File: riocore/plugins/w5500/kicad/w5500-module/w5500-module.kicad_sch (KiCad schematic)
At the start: 2 parts, among them J15 Conn_01x06, J16 Conn_01x06

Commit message: kicad: recover positions
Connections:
- net spi_cs renamed sel
- net spi_miso renamed miso
- net spi_mosi renamed mosi
- net spi_sclk renamed sclk
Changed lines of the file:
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@@
 		)
 	)
-	(hierarchical_label "spi_miso"
+	(hierarchical_label "miso"
 		(shape input)
 		(at 130.81 92.71 180)
@@
 		)
 	)
-	(hierarchical_label "spi_sclk"
+	(hierarchical_label "sclk"
 		(shape input)
 		(at 162.56 97.79 0)
@@
 		)
 	)
-	(hierarchical_label "spi_cs"
+	(hierarchical_label "sel"
 		(shape input)
 		(at 162.56 95.25 0)
@@
 		)
 	)
-	(hierarchical_label "spi_mosi"
+	(hierarchical_label "mosi"
 		(shape input)
 		(at 162.56 100.33 0)

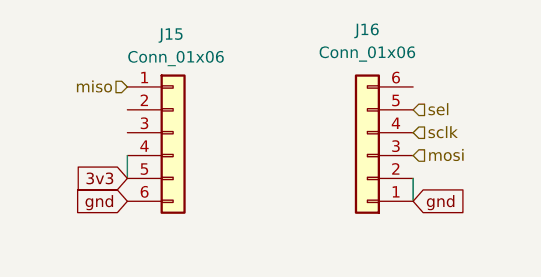
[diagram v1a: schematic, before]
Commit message: kicad: get power-signals
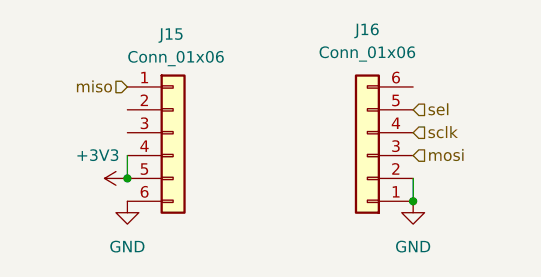
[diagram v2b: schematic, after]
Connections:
- net 3v3 renamed +3V3
- net gnd renamed GND
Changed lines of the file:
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@@
 	(generator_version "9.0")
 	(paper "A4")
+	(junction
+		(at 162.56 105.41)
+		(diameter 0)
+		(color 0 0 0 0)
+	)
+	(junction
+		(at 130.81 102.87)
+		(diameter 0)
+		(color 0 0 0 0)
+	)
 	(wire
 		(pts
@@
 			(width 0)
 			(type default)
-		)
-	)
-	(global_label "gnd"
-		(shape input)
-		(at 162.56 105.41 0)
-		(fields_autoplaced yes)
-		(effects
-			(font
-				(size 1.27 1.27)
-			)
-			(justify left)
-		)
-		(property "Intersheetrefs" "${INTERSHEET_REFS}"
-			(at 168.9128 105.41 0)
-			(effects
-				(font
-					(size 1.27 1.27)
-				)
-				(justify left)
-				(hide yes)
-			)
-		)
-	)
-	(global_label "3v3"
-		(shape input)
-		(at 130.81 102.87 180)
-		(fields_autoplaced yes)
-		(effects
-			(font
-				(size 1.27 1.27)
-			)
-			(justify right)
-		)
-		(property "Intersheetrefs" "${INTERSHEET_REFS}"
-			(at 124.5176 102.87 0)
-			(effects
-				(font
-					(size 1.27 1.27)
-				)
-				(justify right)
-				(hide yes)
-			)
-		)
-	)
-	(global_label "gnd"
-		(shape input)
-		(at 130.81 105.41 180)
-		(fields_autoplaced yes)
-		(effects
-			(font
-				(size 1.27 1.27)
-			)
-			(justify right)
-		)
-		(property "Intersheetrefs" "${INTERSHEET_REFS}"
-			(at 124.4572 105.41 0)
-			(effects
-				(font
-					(size 1.27 1.27)
-				)
-				(justify right)
-				(hide yes)
-			)
 		)
 	)
@@
 			)
 			(justify left)
+		)
+	)
+	(symbol
+		(lib_id "power:GND")
+		(at 130.81 105.41 0)
+		(unit 1)
+		(exclude_from_sim no)
+		(in_bom yes)
+		(on_board yes)
+		(dnp no)
+		(fields_autoplaced yes)
+		(property "Reference" "#PWR01"
+			(at 130.81 111.76 0)
+			(effects
+				(font
+					(size 1.27 1.27)
+				)
+				(hide yes)
+			)
+		)
+		(property "Value" "GND"
+			(at 130.81 110.49 0)
+			(effects
+				(font
+					(size 1.27 1.27)
+				)
+			)
+		)
+		(property "Footprint" ""
+			(at 130.81 105.41 0)
+			(effects
+				(font
+					(size 1.27 1.27)
+				)
+				(hide yes)
+			)
+		)
+		(property "Datasheet" ""
+			(at 130.81 105.41 0)
+			(effects
+				(font
+					(size 1.27 1.27)
+				)
+				(hide yes)
+			)
+		)
+		(property "Description" "Power symbol creates a global label with name \"GND\" , ground"
+			(at 130.81 105.41 0)
+			(effects
+				(font
+					(size 1.27 1.27)
+				)
+				(hide yes)
+			)
+		)
+		(pin "1"
+		)
+		(instances
+			(project "w5500-module"
+				(path "/0f8daeb3-9880-4424-a673-900247e6b186"
+					(reference "#PWR01")
+					(unit 1)
+				)
+			)
 		)
 	)
@@
 					(unit 1)
 				)
+			)
+		)
+	)
+	(symbol
+		(lib_id "power:GND")
+		(at 162.56 105.41 0)
+		(unit 1)
+		(exclude_from_sim no)
+		(in_bom yes)
+		(on_board yes)
+		(dnp no)
+		(fields_autoplaced yes)
+		(property "Reference" "#PWR078"
+			(at 162.56 111.76 0)
+			(effects
+				(font
+					(size 1.27 1.27)
+				)
+				(hide yes)
+			)
+		)
+		(property "Value" "GND"
+			(at 162.56 110.49 0)
+			(effects
+				(font
+					(size 1.27 1.27)
+				)
+			)
+		)
+		(property "Footprint" ""
+			(at 162.56 105.41 0)
+			(effects
+				(font
+					(size 1.27 1.27)
+				)
+				(hide yes)
+			)
+		)
+		(property "Datasheet" ""
+			(at 162.56 105.41 0)
+			(effects
+				(font
+					(size 1.27 1.27)
+				)
+				(hide yes)
+			)
+		)
+		(property "Description" "Power symbol creates a global label with name \"GND\" , ground"
+			(at 162.56 105.41 0)
+			(effects
+				(font
+					(size 1.27 1.27)
+				)
+				(hide yes)
+			)
+		)
+		(pin "1"
+		)
+		(instances
+			(project "w5500-module"
+				(path "/0f8daeb3-9880-4424-a673-900247e6b186"
+					(reference "#PWR078")
+					(unit 1)
+				)
+			)
+		)
+	)
+	(symbol
+		(lib_id "power:+3V3")
+		(at 130.81 102.87 90)
+		(unit 1)
+		(exclude_from_sim no)
+		(in_bom yes)
+		(on_board yes)
+		(dnp no)
+		(property "Reference" "#PWR067"
+			(at 134.62 102.87 0)
+			(effects
+				(font
+					(size 1.27 1.27)
+				)
+				(hide yes)
+			)
+		)
+		(property "Value" "+3V3"
+			(at 127.508 100.33 90)
+			(effects
+				(font
+					(size 1.27 1.27)
+				)
+			)
+		)
+		(property "Footprint" ""
+			(at 130.81 102.87 0)
+			(effects
+				(font
+					(size 1.27 1.27)
+				)
+				(hide yes)
+			)
+		)
+		(property "Datasheet" ""
+			(at 130.81 102.87 0)
+			(effects
+				(font
+					(size 1.27 1.27)
+				)
+				(hide yes)
+			)
+		)
+		(property "Description" "Power symbol creates a global label with name \"+3V3\""
+			(at 130.81 102.87 0)
+			(effects
+				(font
+					(size 1.27 1.27)
+				)
+				(hide yes)
+			)
+		)
+		(pin "1"
+		)
+		(instances
+			(project "w5500-module"
+				(path "/0f8daeb3-9880-4424-a673-900247e6b186"
+					(reference "#PWR067")
+					(unit 1)
+				)
